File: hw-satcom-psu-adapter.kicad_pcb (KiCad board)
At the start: 2 copper layers, 149.7 x 85.2 mm, 84 parts, among them J1 Conn_01x02_Male, J2 ATX-24, J3 Conn_02x02_Top_Bottom, J4 Conn_02x02_Top_Bottom, J5 Conn_01x02_Male, Q1 NCE0140K2, Q2 NCE0140K2, Q3 NCE0140K2, Q4 2N7002, Q5 2N7002, Q6 2N7002, U1 Brick-DCDC, U10 ZXDN10, U2 TPS2350, U3 EL3H7(B)(TA)-G, U4 EL3H7(B)(TA)-G, U5 AV10-48S05, U6 EL3H7(B)(TA)-G, U7 TPS3510, U8 ZXDN10, U9 ZXDN10

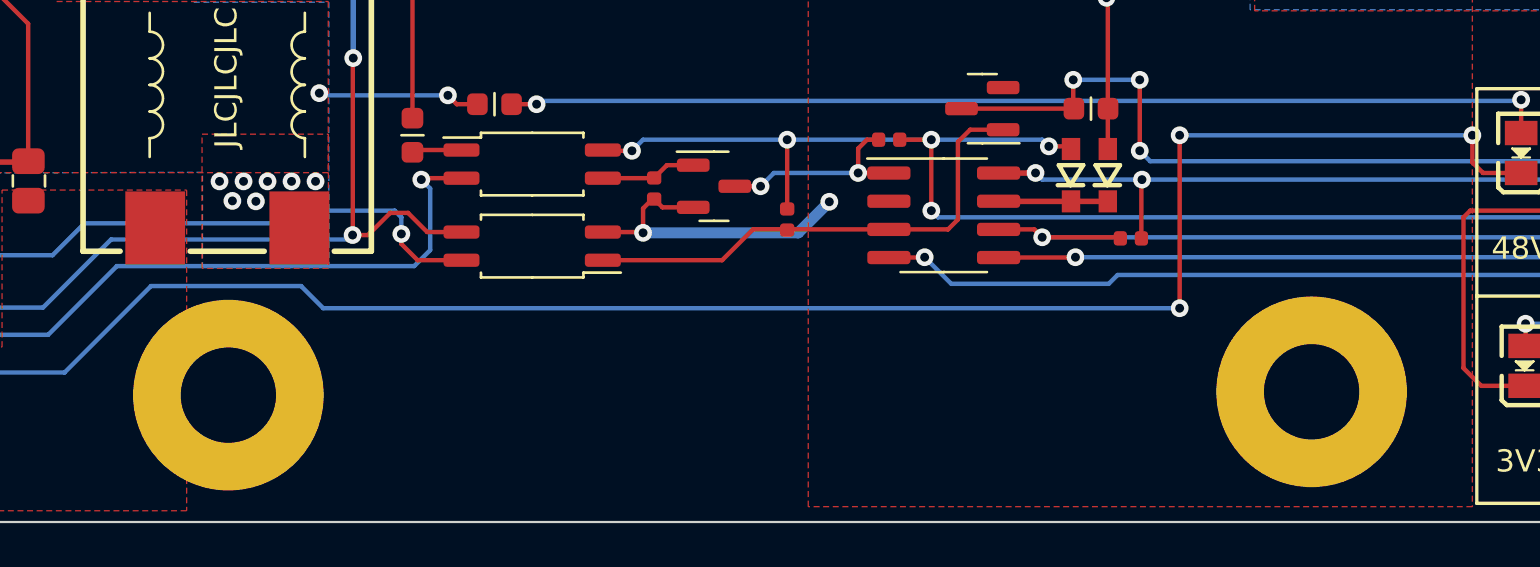
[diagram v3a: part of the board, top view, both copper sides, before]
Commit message: change mounting hole
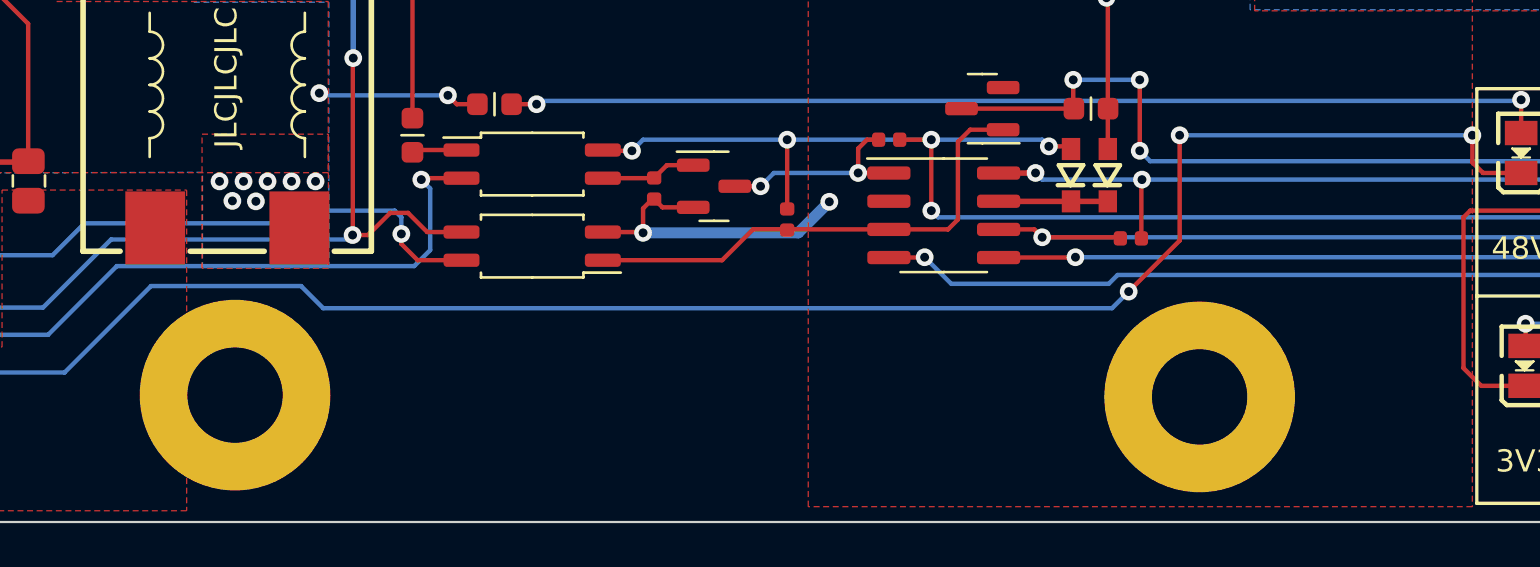
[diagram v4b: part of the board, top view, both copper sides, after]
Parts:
- moved H8 5.06 mm to (166.6, 130.1)
- moved H9 0.30 mm to (123.0, 130.0)
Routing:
- net /NEG: track 122.1 -> 120.3 mm
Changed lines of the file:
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@@
   )
   (footprint "MountingHole:MountingHole_4.3mm_M4_Pad" (layer "F.Cu")
-    (at 122.75 130.02)
+    (at 123.05 130.02)
     (descr "Mounting Hole 4.3mm, M4")
     (tags "mounting hole 4.3mm m4")
@@
   )
   (footprint "MountingHole:MountingHole_4.3mm_M4_Pad" (layer "F.Cu")
-    (at 171.6 129.87)
+    (at 166.55 130.1)
     (descr "Mounting Hole 4.3mm, M4")
     (tags "mounting hole 4.3mm m4")
@@
   (segment (start 104.25 116.2) (end 100.8 116.2) (width 0.2) (layer "F.Cu") (net 54))
   (segment (start 100.8 116.2) (end 100.584 115.984) (width 0.2) (layer "F.Cu") (net 54))
+  (segment (start 163.35 125.3495) (end 165.65 123.0495) (width 0.2) (layer "F.Cu") (net 54))
   (segment (start 178.85 118.3) (end 178.85 119.52) (width 0.2) (layer "F.Cu") (net 54))
   (segment (start 104.476 115.974) (end 104.25 116.2) (width 0.2) (layer "F.Cu") (net 54))
   (segment (start 103.45 111.225) (end 100.375 108.15) (width 0.2) (layer "F.Cu") (net 54))
   (segment (start 100.375 108.15) (end 97.55 108.15) (width 0.2) (layer "F.Cu") (net 54))
-  (segment (start 165.65 126.1) (end 165.65 118.3) (width 0.2) (layer "F.Cu") (net 54))
+  (segment (start 165.65 123.0495) (end 165.65 118.3) (width 0.2) (layer "F.Cu") (net 54))
   (segment (start 104.476 114.7395) (end 104.476 115.974) (width 0.2) (layer "F.Cu") (net 54))
   (via (at 98.1 113.05) (size 0.8) (drill 0.4) (layers "F.Cu" "B.Cu") (net 54))
   (via (at 165.65 118.3) (size 0.8) (drill 0.4) (layers "F.Cu" "B.Cu") (net 54))
-  (via (at 165.65 126.1) (size 0.8) (drill 0.4) (layers "F.Cu" "B.Cu") (net 54))
+  (via (at 163.35 125.3495) (size 0.8) (drill 0.4) (layers "F.Cu" "B.Cu") (net 54))
   (via (at 178.85 118.3) (size 0.8) (drill 0.4) (layers "F.Cu" "B.Cu") (net 54))
-  (segment (start 126.028047 125.1) (end 119.26 125.1) (width 0.2) (layer "B.Cu") (net 54))
-  (segment (start 119.26 125.1) (end 115.36 129) (width 0.2) (layer "B.Cu") (net 54))
-  (segment (start 105.6 123.3) (end 103.8 121.5) (width 0.2) (layer "B.Cu") (net 54))
+  (segment (start 115.36 129) (end 108.15 129) (width 0.2) (layer "B.Cu") (net 54))
+  (segment (start 101.3 121.5) (end 100.43 120.63) (width 0.2) (layer "B.Cu") (net 54))
+  (segment (start 103.8 121.5) (end 101.3 121.5) (width 0.2) (layer "B.Cu") (net 54))
   (segment (start 105.6 126.45) (end 105.6 123.3) (width 0.2) (layer "B.Cu") (net 54))
-  (segment (start 127.028047 126.1) (end 126.028047 125.1) (width 0.2) (layer "B.Cu") (net 54))
-  (segment (start 165.65 126.1) (end 127.028047 126.1) (width 0.2) (layer "B.Cu") (net 54))
-  (segment (start 108.15 129) (end 105.6 126.45) (width 0.2) (layer "B.Cu") (net 54))
+  (segment (start 119.26 125.1) (end 115.36 129) (width 0.2) (layer "B.Cu") (net 54))
   (segment (start 178.85 118.3) (end 165.65 118.3) (width 0.2) (layer "B.Cu") (net 54))
-  (segment (start 100.43 115.38) (end 98.1 113.05) (width 0.2) (layer "B.Cu") (net 54))
-  (segment (start 103.8 121.5) (end 101.3 121.5) (width 0.2) (layer "B.Cu") (net 54))
   (segment (start 100.43 120.63) (end 100.43 115.38) (width 0.2) (layer "B.Cu") (net 54))
-  (segment (start 115.36 129) (end 108.15 129) (width 0.2) (layer "B.Cu") (net 54))
-  (segment (start 101.3 121.5) (end 100.43 120.63) (width 0.2) (layer "B.Cu") (net 54))
+  (segment (start 162.5995 126.1) (end 127.028047 126.1) (width 0.2) (layer "B.Cu") (net 54))
+  (segment (start 100.43 115.38) (end 98.1 113.05) (width 0.2) (layer "B.Cu") (net 54))
+  (segment (start 163.35 125.3495) (end 162.5995 126.1) (width 0.2) (layer "B.Cu") (net 54))
+  (segment (start 108.15 129) (end 105.6 126.45) (width 0.2) (layer "B.Cu") (net 54))
+  (segment (start 127.028047 126.1) (end 126.028047 125.1) (width 0.2) (layer "B.Cu") (net 54))
+  (segment (start 126.028047 125.1) (end 119.26 125.1) (width 0.2) (layer "B.Cu") (net 54))
+  (segment (start 105.6 123.3) (end 103.8 121.5) (width 0.2) (layer "B.Cu") (net 54))
   (segment (start 197.45 131.3) (end 197.05 130.9) (width 0.2) (layer "F.Cu") (net 56))
   (segment (start 197.45 134.1375) (end 197.45 131.3) (width 0.2) (layer "F.Cu") (net 56))
@@
     (connect_pads yes (clearance 0))
     (min_thickness 0.4)
-    (keepout (tracks allowed) (vias allowed) (pads allowed) (copperpour not_allowed) (footprints allowed))
+    (keepout (tracks allowed) (vias allowed) (pads allowed ) (copperpour not_allowed) (footprints allowed))
     (fill (thermal_gap 0.508) (thermal_bridge_width 0.508))
     (polygon
@@
     (connect_pads yes (clearance 0))
     (min_thickness 0.4)
-    (keepout (tracks allowed) (vias allowed) (pads allowed) (copperpour not_allowed) (footprints allowed))
+    (keepout (tracks allowed) (vias allowed) (pads allowed ) (copperpour not_allowed) (footprints allowed))
     (fill (thermal_gap 0.508) (thermal_bridge_width 0.508))
     (polygon

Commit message: TPS2350
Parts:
- added D13: SMCJ60A, Diode_SMD:D_SMC, B.Cu at (94.3, 88.9)
- added D14: SMCJ60A, Diode_SMD:D_SMC, B.Cu at (94.3, 74.7)
- added G***: LOGO, LOGO, F.Cu at (87.8, 159.4)
- added R9: 56k, lc:0603_R, F.Cu at (134.8, 129.4)
- R14: value 120k -> 56k
- R7, R8: value 3.3k -> 4.7k
- moved U3 28.1 mm to (136.4, 126.8)
- moved R13 21.3 mm to (131.0, 126.1), turned to 0 degrees
- moved R16 19.7 mm to (131.1, 124.0), turned to 0 degrees
- moved R1 14.9 mm to (196.3, 129.3), turned to -90 degrees
- moved R7 14.4 mm to (193.1, 115.1)
- moved Q6 14.1 mm to (197.5, 119.1)
- moved D1 9.60 mm to (193.1, 128.7)
- moved D11 9.60 mm to (193.1, 119.1)
- moved Q2 6.61 mm to (106.9, 131.0), turned to 0 degrees
- moved H9 4.17 mm to (118.9, 130.4)
- moved Q1 3.53 mm to (90.0, 102.5), turned to 90 degrees
- moved Q3 3.53 mm to (97.5, 102.5), turned to 90 degrees
- moved C14 2.52 mm to (111.2, 120.4)
- moved FL1 2.10 mm to (120.6, 116.1)
- moved H8 1.04 mm to (167.6, 130.4)
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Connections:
- D4 pad 1: /NEG -> Net-(D4-Pad1)
- Q1 pad 2: /NEG -> /NEGB
- Q1 pad 3: /NEGB -> /NEG
- Q3 pad 2: /NEG -> /NEGA
- Q3 pad 3: /NEGA -> /NEG
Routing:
- net /NEG: track 120.3 -> 16.3 mm, vias 4 -> 0
- net Net-(D4-Pad1): track 0.00 -> 55.5 mm, vias 0 -> 4
- net +12V: track 27.0 -> 73.7 mm, vias 21 -> 25
- net Net-(Q2-Pad3): track 11.0 -> 43.0 mm, vias 0 -> 2
- net GND2: track 88.3 -> 63.4 mm, vias 27 -> 28
- net Net-(R16-Pad2): track 28.6 -> 11.2 mm
- net Net-(R17-Pad2): track 56.5 -> 42.7 mm, vias 3 -> 1
- net /PGOOD: track 104.9 -> 95.9 mm
- net +5VD: track 45.5 -> 41.4 mm, vias 3 -> 1
- net Net-(R13-Pad2): track 5.82 -> 1.77 mm, vias 2 -> 0
- net /NEGB: track 35.1 -> 31.1 mm, vias 2 -> 14
- net /RTN: track 26.4 -> 23.1 mm, vias 9 -> 26
- net +5VA: track 108.6 -> 111.8 mm, vias 4 -> 6
- net Net-(Q2-Pad1): track 7.55 -> 10.6 mm
- net /RTN_FIL: track 53.6 -> 55.9 mm
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- added copper zone on B.Cu, net /NEGA
- added copper zone on B.Cu, net /NEGB

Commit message: LM5067
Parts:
- removed C5: 47nF, lc:0402_C
- removed C6: 10nF, lc:0402_C
- removed D14: SMCJ60A, Diode_SMD:D_SMC
- removed D2: Red, lc:0805_LED_S1_NUM
- removed D3: 1N4148WS, lc:SOD-323
- removed J5: Conn_01x02_Male, Connector_AMASS:AMASS_XT60-M_1x02_P7.20mm_Vertical
- removed Q1, Q3: NCE0140K2, Package_TO_SOT_SMD:TO-252-2
- added C2: 470nF, lc:0402_C, F.Cu at (104.2, 111.6)
- added C3: 100nF, lc:0805_C, F.Cu at (109.0, 114.9)
- added R10: 56k, lc:0402_R, F.Cu at (105.2, 110.3)
- D13: value SMCJ60A -> SMCJ70A; moved to F.Cu
- J1: value Conn_01x02_Male -> XT60
- Q2: value NCE0140K2 -> KIA3510AD
- R11: value 8.2k -> 4.7k
- R12: value 220k -> 10k; footprint lc:0603_R -> lc:1206_R
- R13, R16: footprint lc:0402_R -> lc:0603_R
- R15: value 3m -> 4m
- R5: value 390k -> 130k
- R6: value 5.6k -> 4.7k
- U2: value TPS2350 -> LM5067; footprint Package_SO:TSSOP-14_4.4x5mm_P0.65mm -> Package_SO:MSOP-10_3x3mm_P0.5mm
- moved D13 12.4 mm to (106.5, 91.0), turned to 180 degrees
- moved J1 7.18 mm to (102.7, 81.6)
- moved R12 4.44 mm to (110.4, 111.7), turned to 180 degrees
- moved R6 2.95 mm to (107.3, 109.2)
- moved R5 2.95 mm to (110.9, 109.1)
- moved R11 2.57 mm to (105.2, 109.2), turned to 180 degrees
- moved U2 1.46 mm to (105.9, 116.2)
- moved R9 1.08 mm to (133.8, 129.4)
- moved C14 0.81 mm to (112.0, 120.4)
- moved R16 0.53 mm to (130.5, 123.9)
- moved R13 0.51 mm to (130.5, 126.1), turned to 180 degrees
- moved R18 0.07 mm to (131.0, 118.2), turned to -90 degrees
- turned kibuzzard-62760563 to 180 degrees
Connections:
- D13 pad 2: /NEGA -> VEE
- J1 pad 1: /NEGA -> VEE
- R11 pad 2: /NEG -> VEE
- R12 pad 1: Net-(D2-Pad2) -> /RTN
- R12 pad 2: /RTN -> Net-(C3-Pad2)
- R13 pad 1: /RTN -> Net-(U3-Pad1)
- R13 pad 2: Net-(R13-Pad2) -> /RTN
- R15 pad 2: /NEG -> VEE
- R18 pad 1: Net-(R18-Pad1) -> /RTN
- R18 pad 2: /RTN_FIL -> Net-(R18-Pad2)
- R9 pad 1: Net-(Q2-Pad3) -> /NEG_SS
- U2 pad 1: Net-(D3-Pad1) -> Net-(C3-Pad2)
- U2 pad 10: Net-(Q2-Pad3) -> /PG_HV
- U2 pad 2: Net-(D2-Pad1) -> Net-(R5-Pad2)
- U2 pad 3: Net-(R5-Pad2) -> Net-(R11-Pad1)
- U2 pad 4: Net-(R11-Pad1) -> Net-(R10-Pad2)
- U2 pad 5: Net-(C5-Pad2) -> VEE
- U2 pad 7: /NEG -> Net-(Q2-Pad3)
- U2 pad 8: Net-(U2-Pad8) -> Net-(Q2-Pad1)
- U2 pad 9: Net-(U2-Pad9) -> /NEG_SS
- U3 pad 1: Net-(R13-Pad2) -> Net-(U3-Pad1)
- U6 pad 1: Net-(R18-Pad1) -> Net-(R18-Pad2)
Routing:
- net Net-(Q2-Pad3): track 43.0 -> 9.29 mm, vias 2 -> 0
- net /NEG_SS: track 0.00 -> 32.1 mm
- net /NEGB: track 31.1 -> 0.00 mm, vias 14 -> 0
- net /NEGA: track 28.5 -> 0.00 mm, vias 11 -> 0
- net Net-(U2-Pad8): track 28.0 -> 0.00 mm, vias 2 -> 0
- net Net-(U2-Pad9): track 21.0 -> 0.00 mm, vias 2 -> 0
- net /NEG: track 16.3 -> 0.00 mm
- net /RTN_FIL: track 55.9 -> 41.0 mm
- net VEE: track 0.00 -> 12.0 mm
- net Net-(D2-Pad1): track 6.69 -> 0.00 mm, vias 2 -> 0
- net Net-(C3-Pad2): track 0.00 -> 6.50 mm
- net Net-(C2-Pad1): track 3.73 -> 10.0 mm, vias 0 -> 2
- net /RTN: track 23.1 -> 18.6 mm, vias 26 -> 22
- net Net-(R10-Pad2): track 0.00 -> 3.81 mm
- net Net-(D3-Pad1): track 3.73 -> 0.00 mm
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- added copper zone on F.Cu, net VEE
- removed copper zone on F.Cu, net /NEG
- removed copper zone on B.Cu, net /NEGA
- removed copper zone on F.Cu, net /NEGA
- removed copper zone on B.Cu, net /NEGB
- removed copper zone on F.Cu, net /NEGB
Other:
- board text added: "JLCJLCJLCJLC"
- board text removed: "A"
- board text removed: "B"
- board text removed: "JLCJLCJLC"

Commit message: Layout improvements
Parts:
- moved C9 66.1 mm to (110.5, 54.4), turned to 0 degrees
- moved C7 2.53 mm to (198.2, 70.0), turned to 0 degrees
- moved C8 2.04 mm to (190.0, 70.0), turned to 0 degrees
- moved C10 1.54 mm to (181.9, 70.0), turned to 0 degrees
- moved J_CPU2 0.70 mm to (179.8, 59.4)
- moved C15 0.19 mm to (217.4, 69.4)
- moved C16 0.18 mm to (217.5, 79.2), turned to 90 degrees
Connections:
- J_CPU1 pad 1: GND2 -> +12V
- J_CPU1 pad 2: GND2 -> +12V
- J_CPU1 pad 3: GND2 -> +12V
- J_CPU1 pad 4: GND2 -> +12V
- J_CPU1 pad 5: +12V -> GND2
- J_CPU1 pad 6: +12V -> GND2
- J_CPU1 pad 7: +12V -> GND2
- J_CPU1 pad 8: +12V -> GND2
- J_CPU2 pad 1: GND2 -> +12V
- J_CPU2 pad 2: GND2 -> +12V
- J_CPU2 pad 3: GND2 -> +12V
- J_CPU2 pad 4: GND2 -> +12V
- J_CPU2 pad 5: +12V -> GND2
- J_CPU2 pad 6: +12V -> GND2
- J_CPU2 pad 7: +12V -> GND2
- J_CPU2 pad 8: +12V -> GND2
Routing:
- net +12V: track 73.7 -> 120.8 mm
- net /+5VSB: track 300.1 -> 267.6 mm
- net /DCDC_EN: track 168.4 -> 186.1 mm, vias 13 -> 11
- added copper zone on B.Cu, net /+5VSB
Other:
- board text added: "Lenovo H81 SATA cable"
- board text added: "Seasonic KM3 PCIe / CPU cable"
- board text removed: "HDD Power"

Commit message: Fix
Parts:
- removed Q4: 2N7002, Package_TO_SOT_SMD:SOT-23
- added C11: 100nF/100V, lc:0805_C, F.Cu at (106.4, 96.5)
- added C4: 100nF/100V, lc:0805_C, F.Cu at (121.4, 96.0)
- added C5: 100nF/100V, lc:0805_C, F.Cu at (127.9, 66.0)
- added C6: 100nF/100V, lc:0805_C, F.Cu at (152.9, 116.7)
- added R28: 100k, lc:0402_R, F.Cu at (149.9, 123.7)
- D1, D10, D11, D12, D4, D5, D8, D9: footprint lc:0805_LED_S1_NUM -> lc:0603_LED_S1_NUM
- H2, H3, H8, H9: footprint MountingHole:MountingHole_4.3mm_M4_Pad -> t123yh:MountingHole_SMTSO-M3
- H4, H5, H6, H7: footprint MountingHole:MountingHole_5.5mm_Pad -> t123yh:MountingHole_SMTSO-632
- J_CPU1, J_CPU2: footprint t123yh:ATX-8P -> t123yh:ATX-8P-Square
- R13: value 51k -> 27k; footprint lc:0603_R -> lc:0805_R
- R16: value 10k -> 1k
- R17: value 220k -> 1k
- R18: value 51k -> 5.1k; footprint lc:0603_R -> lc:0402_R
- R20: value 5.1k -> 3.3k
- R21: value 5.1k -> 10k
- R7, R8: value 4.7k -> 5.1k
- moved R22 100.4 mm to (104.9, 54.9), turned to 90 degrees
- moved D1 95.4 mm to (112.3, 78.0)
- moved D10 95.4 mm to (108.3, 78.0)
- moved D8 95.4 mm to (100.4, 78.0)
- moved D9 95.4 mm to (104.4, 78.0)
- moved D11 94.2 mm to (112.3, 70.6)
- moved D12 94.2 mm to (108.3, 70.6)
- moved D4 94.2 mm to (100.3, 70.6)
- moved D5 94.2 mm to (104.3, 70.6)
- moved R3 92.0 mm to (119.1, 75.4), turned to 0 degrees
- moved R4 89.2 mm to (123.2, 76.2), turned to 0 degrees
- moved R7 86.5 mm to (119.8, 69.0), turned to 0 degrees
- moved R8 83.8 mm to (119.8, 67.8), turned to 0 degrees
- moved R14 63.3 mm to (91.5, 70.6), turned to -90 degrees
- moved Q6 41.2 mm to (156.8, 112.8)
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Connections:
- C14 pad 2: /NEG_SS -> GND1
- FL1 pad 1: /NEG_SS -> GND1
- Q2 pad 2: /NEG_SS -> GND1
- Q5 pad 1: /FPO -> Net-(Q5-Pad1)
- R1 pad 1: Net-(D1-Pad2) -> Net-(D8-Pad2)
- R13 pad 1: Net-(U3-Pad1) -> /PG_HV
- R16 pad 1: /RTN -> Net-(R16-Pad1)
- R16 pad 2: Net-(R16-Pad2) -> /PG_HV
- R17 pad 1: /NEG_FIL -> Net-(R17-Pad1)
- R17 pad 2: Net-(R17-Pad2) -> /PG_HV
- R18 pad 1: /RTN -> /+5VSB
- R18 pad 2: Net-(R18-Pad2) -> /FPO
- R19 pad 1: Net-(Q4-Pad1) -> Net-(R19-Pad1)
- R2 pad 1: Net-(D8-Pad2) -> Net-(D1-Pad2)
- R20 pad 2: /FPO -> Net-(R20-Pad2)
- R21 pad 2: Net-(Q4-Pad3) -> Net-(R21-Pad2)
- R9 pad 1: /NEG_SS -> GND1
- U1 pad GATE: Net-(R17-Pad2) -> /GATE
- U2 pad 9: /NEG_SS -> GND1
- U3 pad 1: Net-(U3-Pad1) -> Net-(R16-Pad1)
- U3 pad 2: /PG_HV -> VEE
- U3 pad 3: Net-(R17-Pad2) -> Net-(U3-Pad3)
- U3 pad 4: Net-(R16-Pad2) -> /GATE
- U4 pad 1: /FPO -> Net-(R20-Pad2)
- U4 pad 2: GND2 -> /FPO
- U4 pad 3: Net-(R17-Pad2) -> GND1
- U4 pad 4: Net-(R16-Pad2) -> Net-(U3-Pad3)
- U6 pad 1: Net-(R18-Pad2) -> Net-(R17-Pad1)
- U6 pad 2: /PG_HV -> VEE
- U6 pad 3: Net-(Q4-Pad1) -> Net-(R19-Pad1)
- U6 pad 4: /+5VSB -> Net-(R21-Pad2)
- U7 pad 1: Net-(Q4-Pad3) -> Net-(R19-Pad1)
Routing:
- net +5VD: track 41.4 -> 144.3 mm, vias 1 -> 3
- net /PSON: track 125.7 -> 213.8 mm
- net Net-(D1-Pad2): track 3.74 -> 84.3 mm, vias 0 -> 2
- net +5VA: track 111.8 -> 186.4 mm
- net Net-(D8-Pad2): track 18.8 -> 92.3 mm
- net Net-(D11-Pad1): track 7.59 -> 78.4 mm, vias 0 -> 2
- net VEE: track 12.0 -> 60.7 mm, vias 0 -> 4
- net +12V: track 120.8 -> 72.6 mm, vias 25 -> 21
- net Net-(R17-Pad2): track 42.7 -> 0.00 mm, vias 1 -> 0
- net GND1: track 0.00 -> 42.3 mm, vias 0 -> 2
- net /GATE: track 0.00 -> 39.5 mm, vias 0 -> 1
- net Net-(D4-Pad2): track 47.1 -> 8.73 mm, vias 2 -> 0
- net /NEG_SS: track 32.1 -> 0.00 mm
- net Net-(D4-Pad1): track 56.6 -> 87.6 mm, vias 4 -> 2
- net Net-(Q5-Pad1): track 0.00 -> 24.7 mm, vias 0 -> 4
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- added copper zone on F.Cu, net GND1
- added copper zone on B.Cu, net VEE
- removed copper zone on F.Cu, net /NEG_SS
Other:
- board size 149.7 x 85.2 mm -> 148.9 x 85.2 mm
- board text added: "(+)"
- board text added: "(-)"
- board text added: "3.3V"
- board text added: "E"
- board text added: "G"
- board text added: "N"
- board text added: "R"
- board text added: "T"
- board text removed: "Lenovo H81 SATA cable"
- board text removed: "NEG (-)"
- board text removed: "RTN (+)"
- board text removed: "Seasonic KM3 PCIe / CPU cable"
